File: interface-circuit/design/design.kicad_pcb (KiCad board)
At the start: 2 copper layers, 126.8 x 83.8 mm, 23 parts, among them J10 FAN_RELAY, J11 Conn_Switch, J12 Conn_Reset, J2 Screw_Term_RPi, J3 Screw_Term_Detector, J4 12V_IN, J5 Conn_Pwr_LED, J6 Conn_Piezo, J7 Conn_Printer_Mode, J8 Conn_Fan_Mode, J9 PRINTER_RELAY, Q1 2N3904-AP, Q2 2N3904-AP, Q3 2N3904-AP, U1 LogicLevelConverter_BOB-08745

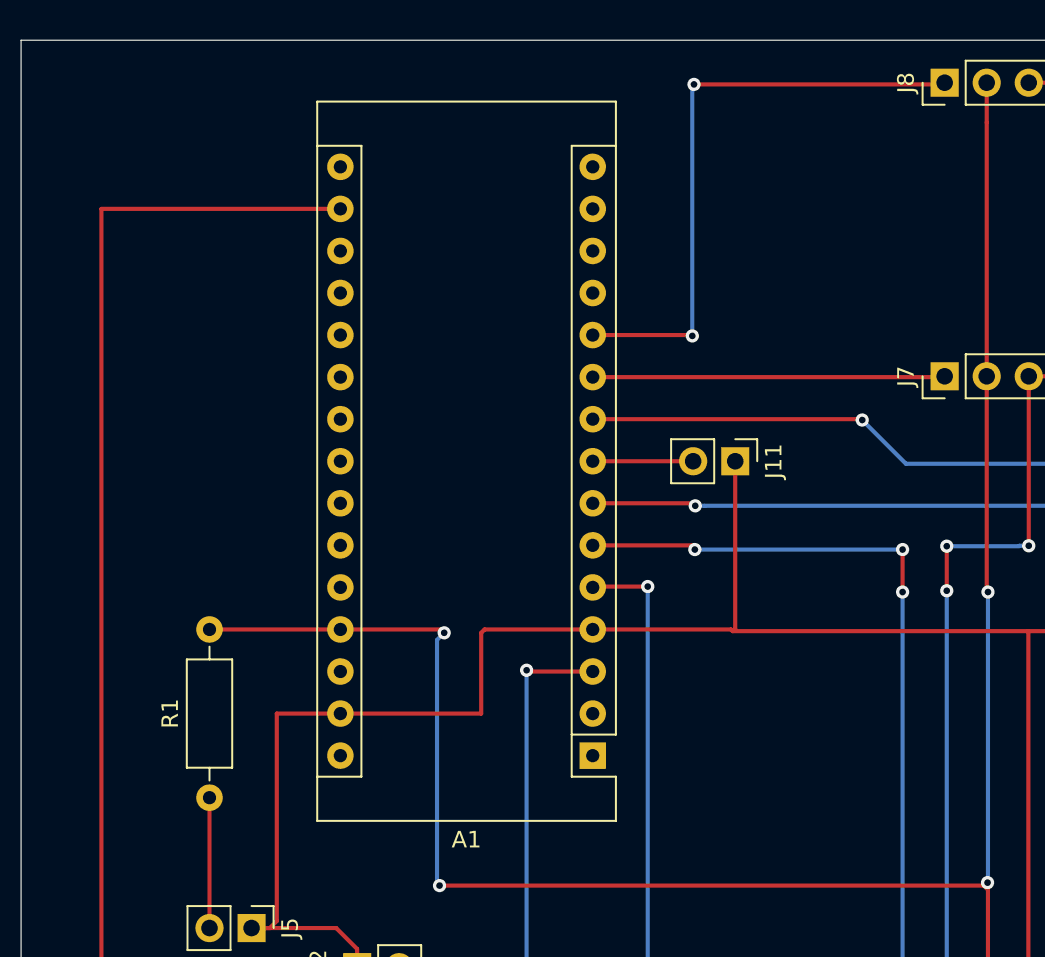
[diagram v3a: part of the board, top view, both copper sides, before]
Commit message: Aligned nano on board
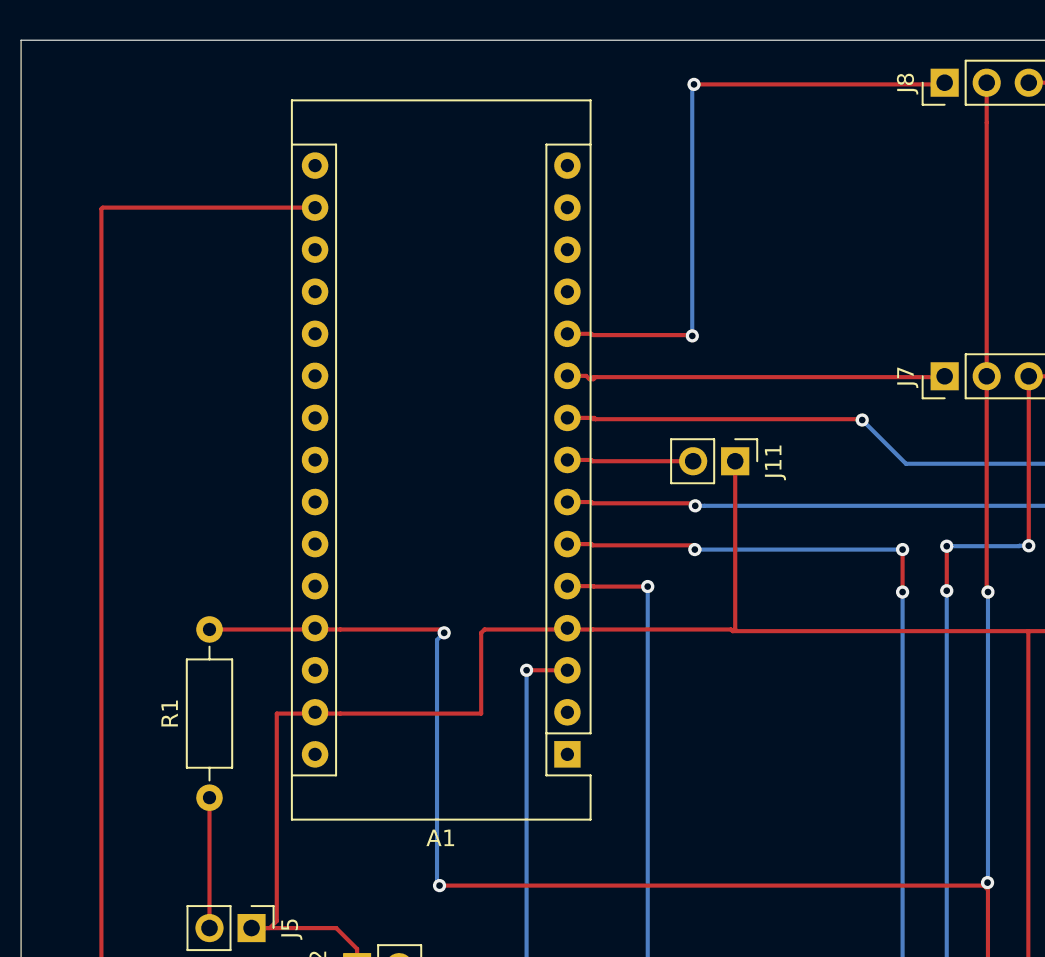
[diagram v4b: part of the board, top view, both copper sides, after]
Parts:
- moved A1 1.53 mm to (55.9, 119.3)
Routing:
- net /D7_PRINTER_RELAY: track 21.3 -> 23.1 mm
- net /HV_AlarmTriggered: track 78.4 -> 80.1 mm
- net /SOFT_SWITCH: track 6.06 -> 7.63 mm
- net /HV_PrinterPowerDemand: track 46.3 -> 47.8 mm
- net /HV_FanPowerDemand: track 65.0 -> 66.6 mm
- net /D8_FAN_RELAY: track 36.4 -> 38.0 mm
- net +3V3: track 124.6 -> 123.1 mm
- net /RESET: track 29.5 -> 28.1 mm
- net /DETECTOR_SIGNAL: track 130.6 -> 131.7 mm
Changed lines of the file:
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@@
     (thickness 1.6)
     (drawings 4)
-    (tracks 229)
+    (tracks 246)
     (zones 0)
     (modules 23)
@@
   )
   (module Module:Arduino_Nano (layer F.Cu)
-    (at 57.435001 119.38 180)
+    (at 55.9054 119.3038 180)
     (descr "Arduino Nano, http://www.mouser.com/pdfdocs/Gravitech_Arduino_Nano3_0.pdf")
     (tags "Arduino Nano")
@@
   (gr_line (start 149.7584 76.1746) (end 149.7584 159.9692) (layer Edge.Cuts) (width 0.05))
   (gr_line (start 22.9108 76.1746) (end 149.7584 76.1746) (layer Edge.Cuts) (width 0.05))
-  (segment (start 42.195001 86.36) (end 27.7622 86.36) (width 0.25) (layer F.Cu) (net 2))
   (segment (start 27.7622 86.36) (end 27.7622 142.0114) (width 0.25) (layer F.Cu) (net 2))
   (segment (start 78.867 142.0114) (end 81.3054 144.4498) (width 0.25) (layer F.Cu) (net 2))
   (segment (start 27.7622 142.0114) (end 78.867 142.0114) (width 0.25) (layer F.Cu) (net 2))
+  (segment (start 27.8384 86.2838) (end 40.6654 86.2838) (width 0.25) (layer F.Cu) (net 2))
+  (segment (start 27.7622 86.36) (end 27.8384 86.2838) (width 0.25) (layer F.Cu) (net 2))
   (via (at 53.4416 114.2238) (size 0.8) (drill 0.4) (layers F.Cu B.Cu) (net 5))
-  (segment (start 57.435001 114.3) (end 53.5178 114.3) (width 0.25) (layer F.Cu) (net 5))
   (segment (start 53.5178 114.3) (end 53.4416 114.2238) (width 0.25) (layer F.Cu) (net 5))
   (segment (start 53.4416 114.2238) (end 53.4416 131.953) (width 0.25) (layer B.Cu) (net 5))
@@
   (segment (start 53.2384 132.1562) (end 53.4416 131.953) (width 0.25) (layer F.Cu) (net 5))
   (segment (start 45.7454 132.1562) (end 53.2384 132.1562) (width 0.25) (layer F.Cu) (net 5))
+  (segment (start 55.9054 114.2238) (end 53.4416 114.2238) (width 0.25) (layer F.Cu) (net 5))
   (segment (start 42.195001 116.84) (end 38.354 116.84) (width 0.25) (layer F.Cu) (net 7))
   (segment (start 37.93 129.794) (end 36.83 129.794) (width 0.25) (layer F.Cu) (net 7))
@@
   (segment (start 66.04 111.7092) (end 65.8876 111.8616) (width 0.25) (layer F.Cu) (net 7))
   (segment (start 66.04 101.6) (end 66.04 111.7092) (width 0.25) (layer F.Cu) (net 7))
-  (segment (start 57.181001 109.474) (end 57.435001 109.22) (width 0.25) (layer F.Cu) (net 9))
   (segment (start 146.7612 144.8562) (end 142.3924 144.8562) (width 0.25) (layer F.Cu) (net 9))
   (via (at 137.541 149.7076) (size 0.8) (drill 0.4) (layers F.Cu B.Cu) (net 9))
@@
   (segment (start 63.5254 149.5806) (end 60.7568 146.812) (width 0.25) (layer B.Cu) (net 9))
   (segment (start 60.7568 146.812) (end 60.7568 109.1692) (width 0.25) (layer B.Cu) (net 9))
-  (segment (start 57.485801 109.1692) (end 57.435001 109.22) (width 0.25) (layer F.Cu) (net 9))
   (segment (start 60.7568 109.1692) (end 57.485801 109.1692) (width 0.25) (layer F.Cu) (net 9))
+  (segment (start 57.460401 109.1438) (end 55.9054 109.1438) (width 0.25) (layer F.Cu) (net 9))
+  (segment (start 57.485801 109.1692) (end 57.460401 109.1438) (width 0.25) (layer F.Cu) (net 9))
   (segment (start 57.435001 106.68) (end 63.4746 106.68) (width 0.25) (layer F.Cu) (net 11))
   (via (at 63.6016 106.934) (size 0.8) (drill 0.4) (layers F.Cu B.Cu) (net 11))
@@
   (segment (start 76.1492 134.2136) (end 76.2254 134.2898) (width 0.25) (layer B.Cu) (net 11))
   (segment (start 76.1492 109.4994) (end 76.1492 134.2136) (width 0.25) (layer B.Cu) (net 11))
+  (segment (start 57.358801 106.6038) (end 55.9054 106.6038) (width 0.25) (layer F.Cu) (net 11))
+  (segment (start 57.435001 106.68) (end 57.358801 106.6038) (width 0.25) (layer F.Cu) (net 11))
   (via (at 63.627 104.2924) (size 0.8) (drill 0.4) (layers F.Cu B.Cu) (net 13))
   (segment (start 57.435001 104.14) (end 63.4746 104.14) (width 0.25) (layer F.Cu) (net 13))
@@
   (segment (start 88.9254 129.4384) (end 88.9254 134.2898) (width 0.25) (layer F.Cu) (net 13))
   (segment (start 91.4654 126.8984) (end 88.9254 129.4384) (width 0.25) (layer F.Cu) (net 13))
+  (segment (start 57.358801 104.0638) (end 55.9054 104.0638) (width 0.25) (layer F.Cu) (net 13))
+  (segment (start 57.435001 104.14) (end 57.358801 104.0638) (width 0.25) (layer F.Cu) (net 13))
   (segment (start 63.5 101.6) (end 57.435001 101.6) (width 0.25) (layer F.Cu) (net 15))
+  (segment (start 57.358801 101.5238) (end 55.9054 101.5238) (width 0.25) (layer F.Cu) (net 15))
+  (segment (start 57.435001 101.6) (end 57.358801 101.5238) (width 0.25) (layer F.Cu) (net 15))
   (via (at 73.7108 99.1108) (size 0.8) (drill 0.4) (layers F.Cu B.Cu) (net 17))
-  (segment (start 57.435001 99.06) (end 73.66 99.06) (width 0.25) (layer F.Cu) (net 17))
   (segment (start 73.66 99.06) (end 73.7108 99.1108) (width 0.25) (layer F.Cu) (net 17))
   (via (at 88.9508 101.7524) (size 0.8) (drill 0.4) (layers F.Cu B.Cu) (net 17))
@@
   (segment (start 88.9508 104.2416) (end 88.9508 101.7524) (width 0.25) (layer F.Cu) (net 17))
   (segment (start 86.5124 106.68) (end 88.9508 104.2416) (width 0.25) (layer F.Cu) (net 17))
+  (segment (start 57.531 98.9838) (end 55.9054 98.9838) (width 0.25) (layer F.Cu) (net 17))
+  (segment (start 57.6072 99.06) (end 57.531 98.9838) (width 0.25) (layer F.Cu) (net 17))
+  (segment (start 57.6072 99.06) (end 73.66 99.06) (width 0.25) (layer F.Cu) (net 17))
+  (segment (start 57.435001 99.06) (end 57.6072 99.06) (width 0.25) (layer F.Cu) (net 17))
   (segment (start 78.6384 96.52) (end 78.6892 96.4692) (width 0.25) (layer F.Cu) (net 19))
-  (segment (start 57.435001 96.52) (end 78.6384 96.52) (width 0.25) (layer F.Cu) (net 19))
+  (segment (start 57.03677 96.4438) (end 57.23997 96.647) (width 0.25) (layer F.Cu) (net 19))
+  (segment (start 55.9054 96.4438) (end 57.03677 96.4438) (width 0.25) (layer F.Cu) (net 19))
+  (segment (start 57.4802 96.647) (end 57.6072 96.52) (width 0.25) (layer F.Cu) (net 19))
+  (segment (start 57.23997 96.647) (end 57.4802 96.647) (width 0.25) (layer F.Cu) (net 19))
+  (segment (start 57.435001 96.52) (end 57.6072 96.52) (width 0.25) (layer F.Cu) (net 19))
+  (segment (start 57.6072 96.52) (end 78.6384 96.52) (width 0.25) (layer F.Cu) (net 19))
   (via (at 63.4492 94.0308) (size 0.8) (drill 0.4) (layers F.Cu B.Cu) (net 21))
   (segment (start 57.435001 93.98) (end 63.3984 93.98) (width 0.25) (layer F.Cu) (net 21))
@@
   (segment (start 78.5876 78.8416) (end 78.6892 78.74) (width 0.25) (layer F.Cu) (net 21))
   (segment (start 63.5508 78.8416) (end 78.5876 78.8416) (width 0.25) (layer F.Cu) (net 21))
+  (segment (start 57.358801 93.9038) (end 55.9054 93.9038) (width 0.25) (layer F.Cu) (net 21))
+  (segment (start 57.435001 93.98) (end 57.358801 93.9038) (width 0.25) (layer F.Cu) (net 21))
   (segment (start 42.195001 111.76) (end 34.29 111.76) (width 0.25) (layer F.Cu) (net 22))
   (via (at 81.2546 139.5984) (size 0.8) (drill 0.4) (layers F.Cu B.Cu) (net 22))

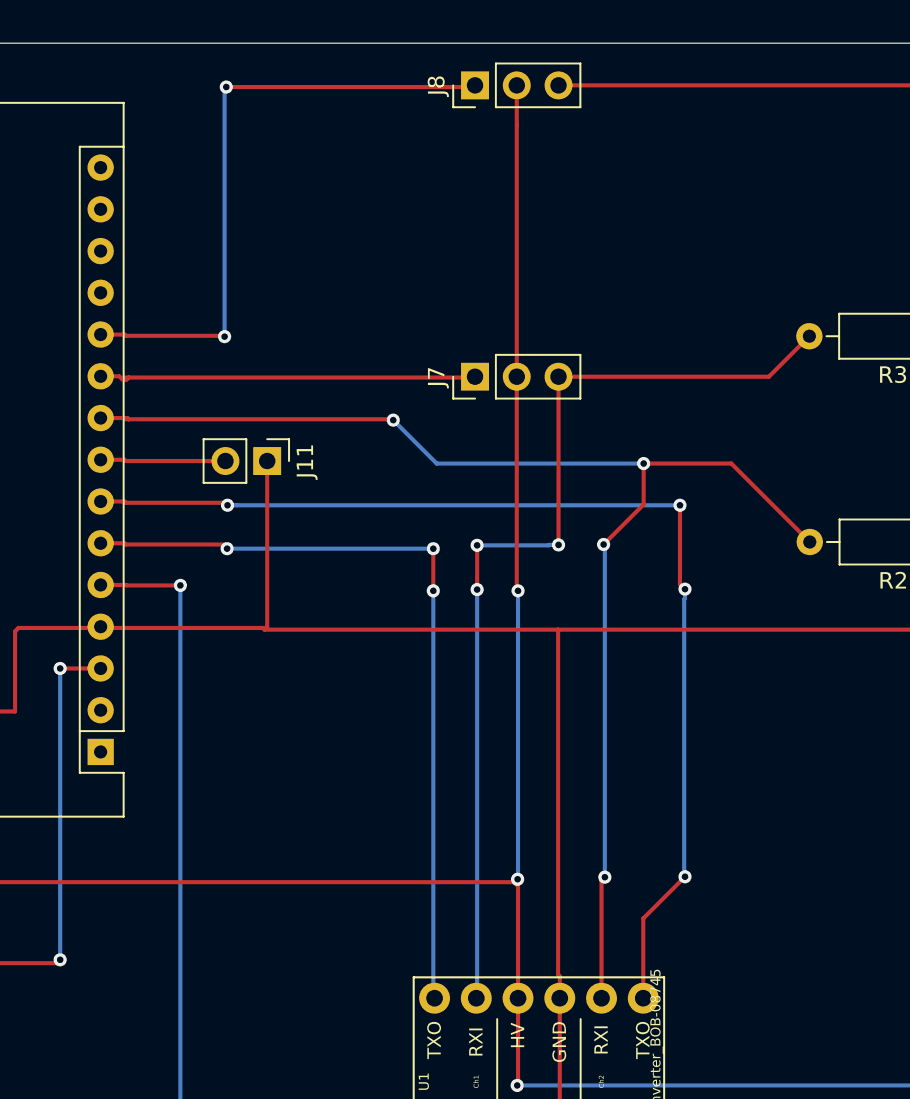
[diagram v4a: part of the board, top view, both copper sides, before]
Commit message: Move printer power demand and relay output to analoge pins to distribute the traces across the board
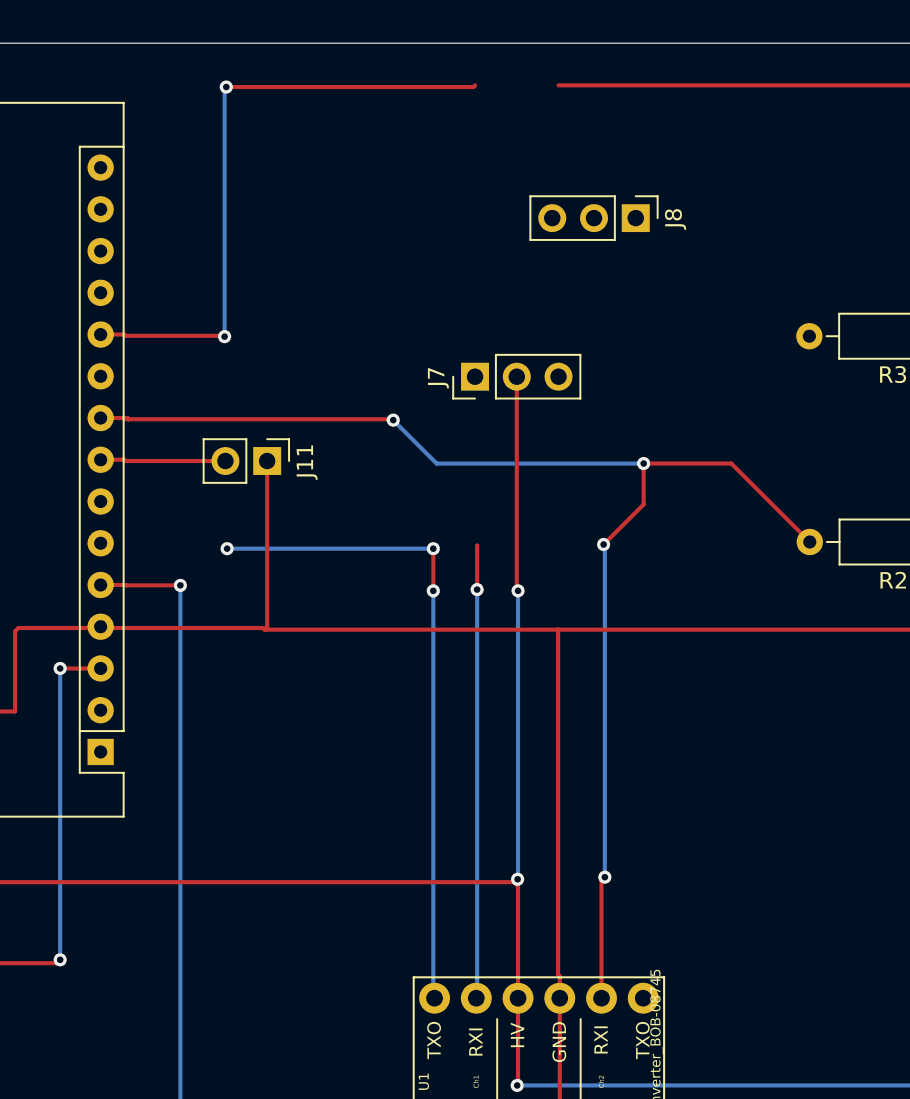
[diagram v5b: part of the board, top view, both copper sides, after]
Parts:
- moved J8 12.7 mm to (88.5, 86.8), turned to 270 degrees
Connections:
- A1 pad 6: /HV_PrinterPowerDemand -> /SW_PRINTER_RELAY
- A1 pad 7: /HV_FanPowerDemand -> /SW_FAN_RELAY
- J7 pad 1: /D7_PRINTER_RELAY -> /HV_PrinterPowerDemand
- J7 pad 3: /HV_PrinterPowerStatus -> /SW_PRINTER_RELAY
- J8 pad 1: /D8_FAN_RELAY -> /HV_FanPowerDemand
- R3 pad 2: /HV_PrinterPowerStatus -> /D7_PRINTER_RELAY
- R4 pad 2: /SW_FAN_RELAY -> /D8_FAN_RELAY
- U1 pad 1: /HV_PrinterPowerStatus -> /D7_PRINTER_RELAY
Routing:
- net /HV_FanPowerDemand: track 66.6 -> 0.00 mm, vias 4 -> 0
- net /HV_PrinterPowerStatus: track 59.1 -> 0.00 mm, vias 3 -> 0
- net /SW_FAN_RELAY: track 22.9 -> 0.00 mm
- net /D8_FAN_RELAY: track 38.0 -> 60.9 mm
- net +5V: track 194.1 -> 176.3 mm
- net /HV_PrinterPowerDemand: track 47.8 -> 40.3 mm
- net /D7_PRINTER_RELAY: track 23.1 -> 27.6 mm, vias 0 -> 1
